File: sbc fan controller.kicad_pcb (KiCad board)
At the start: 2 copper layers, 46 x 53 mm, 23 parts, among them J1 Conn_01x13, J10 ISP-6, J2 Conn_01x02, J3 TEST_1P, J6 Conn_01x03, J7 TEST_1P, Q1 Q_PMOS_GSD, U1 ATTINY13A-SSU, U3 4N25

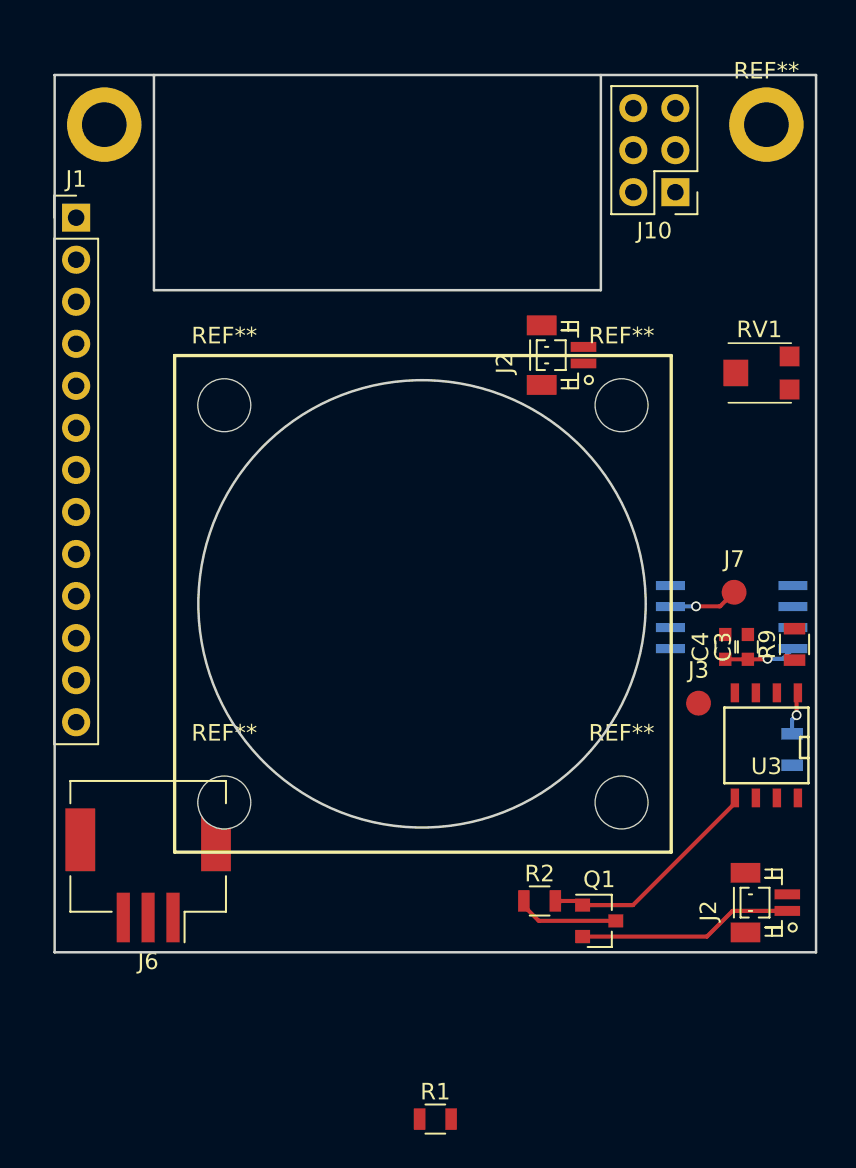
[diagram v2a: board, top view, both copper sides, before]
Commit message: Final layout
Simplified layout and tested each footprint with a hard copy layout actual parts.
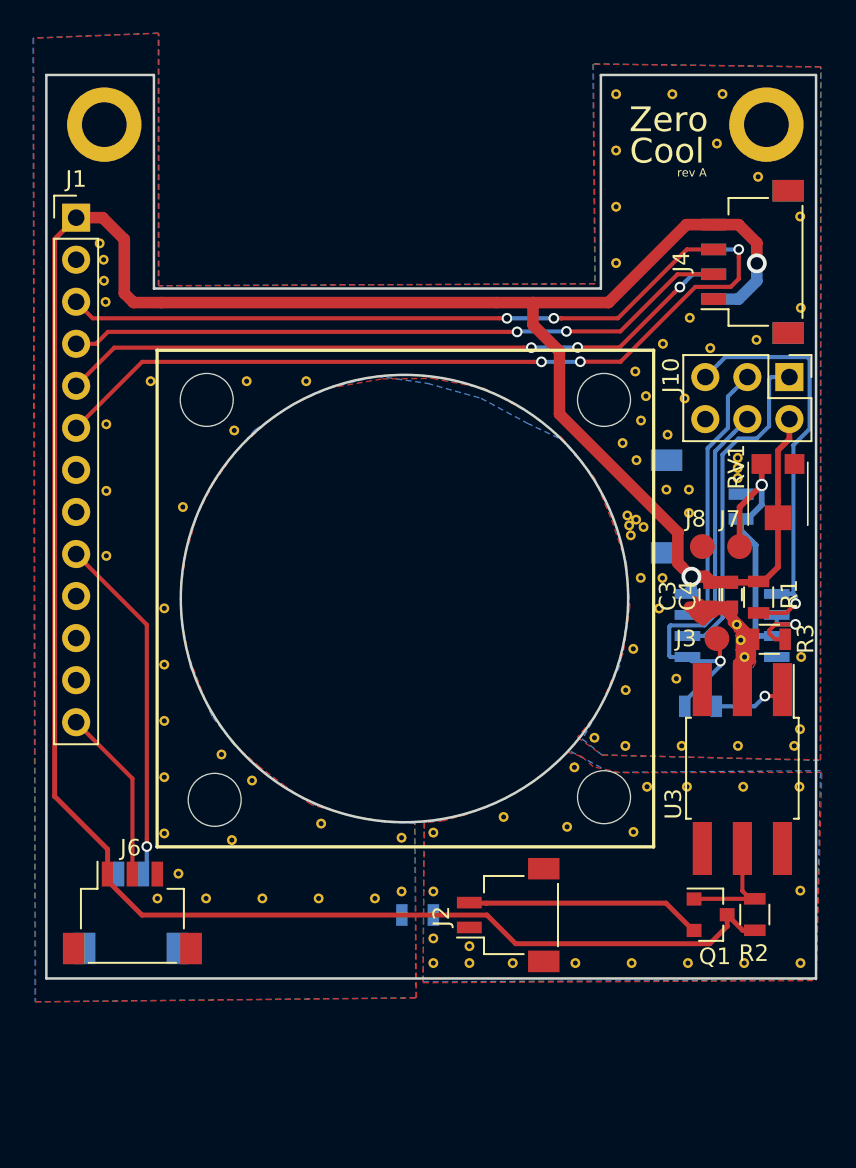
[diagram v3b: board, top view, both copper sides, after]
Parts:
- removed the J2 at (190.7, 56.9)
- removed the J2 at (203.0, 90.0)
- removed R9: 0R, Resistors_SMD:R_0805
- added J2: Conn_01x02, JST_test_2:JST_ZH_SM02B-ZRSS-TB_1x02_P1.50mm_Horizontal, F.Cu at (187.4, 90.8)
- added J4: Conn_01x04, JST_test_2:JST_ZH_SM04B-ZRSS-TB_1x04_P1.50mm_Horizontal, F.Cu at (202.2, 51.3)
- added J5: Conn_01x04, JST_test_2:JST_ZH_SM04B-ZRSS-TB_1x04_P1.50mm_Horizontal, B.Cu at (202.2, 51.3)
- added J8: TEST_1P, Measurement_Points:Measurement_Point_Round-SMD-Pad_Small, F.Cu at (199.1, 68.5)
- added J9: Conn_01x02, JST_test_2:JST_ZH_SM02B-ZRSS-TB_1x02_P1.50mm_Horizontal, B.Cu at (164.6, 90.6)
- added L1: Ferrite_Bead, Resistors_SMD:R_0805, B.Cu at (181.9, 90.8)
- added R3: 10k, Resistors_SMD:R_0805, F.Cu at (203.2, 74.1)
- added REF**: VIA-0.6mm, node_nrf:VIA-0.6mm, F.Cu at (201.2, 73.2)
- added REF**: VIA-0.6mm, node_nrf:VIA-0.6mm, F.Cu at (163.0, 52.4)
- added REF**: VIA-0.6mm, node_nrf:VIA-0.6mm, F.Cu at (205.1, 93.7)
- added REF**: VIA-0.6mm, node_nrf:VIA-0.6mm, F.Cu at (185.1, 93.7)
- added REF**: VIA-0.6mm, node_nrf:VIA-0.6mm, F.Cu at (185.1, 92.6)
- added REF**: VIA-0.6mm, node_nrf:VIA-0.6mm, F.Cu at (166.2, 89.8)
- added REF**: VIA-0.6mm, node_nrf:VIA-0.6mm, F.Cu at (163.1, 53.7)
- added REF**: VIA-0.6mm, node_nrf:VIA-0.6mm, F.Cu at (163.1, 65.1)
- added REF**: VIA-0.6mm, node_nrf:VIA-0.6mm, F.Cu at (163.1, 69.0)
- added REF**: VIA-0.6mm, node_nrf:VIA-0.6mm, F.Cu at (167.8, 66.1)
- added REF**: VIA-0.6mm, node_nrf:VIA-0.6mm, F.Cu at (170.8, 61.5)
- added REF**: VIA-0.6mm, node_nrf:VIA-0.6mm, F.Cu at (175.2, 58.5)
- added REF**: VIA-0.6mm, node_nrf:VIA-0.6mm, F.Cu at (201.4, 74.1)
- added REF**: VIA-0.6mm, node_nrf:VIA-0.6mm, F.Cu at (171.6, 58.5)
- added REF**: VIA-0.6mm, node_nrf:VIA-0.6mm, F.Cu at (165.8, 58.5)
- added REF**: VIA-0.6mm, node_nrf:VIA-0.6mm, F.Cu at (163.1, 61.1)
- added REF**: VIA-0.6mm, node_nrf:VIA-0.6mm, F.Cu at (166.6, 72.2)
- added REF**: VIA-0.6mm, node_nrf:VIA-0.6mm, F.Cu at (166.6, 75.6)
- added REF**: VIA-0.6mm, node_nrf:VIA-0.6mm, F.Cu at (166.6, 79.0)
- added REF**: VIA-0.6mm, node_nrf:VIA-0.6mm, F.Cu at (166.6, 82.4)
- added REF**: VIA-0.6mm, node_nrf:VIA-0.6mm, F.Cu at (166.6, 85.8)
- added REF**: VIA-0.6mm, node_nrf:VIA-0.6mm, F.Cu at (167.5, 88.2)
- added REF**: VIA-0.6mm, node_nrf:VIA-0.6mm, F.Cu at (170.1, 81.0)
- added REF**: VIA-0.6mm, node_nrf:VIA-0.6mm, F.Cu at (201.7, 75.2)
- added REF**: VIA-0.6mm, node_nrf:VIA-0.6mm, F.Cu at (170.7, 86.2)
- added REF**: VIA-0.6mm, node_nrf:VIA-0.6mm, F.Cu at (169.2, 89.7)
- added REF**: VIA-0.6mm, node_nrf:VIA-0.6mm, F.Cu at (172.6, 89.7)
- added REF**: VIA-0.6mm, node_nrf:VIA-0.6mm, F.Cu at (175.9, 89.7)
- added REF**: VIA-0.6mm, node_nrf:VIA-0.6mm, F.Cu at (171.9, 82.6)
- added REF**: VIA-0.6mm, node_nrf:VIA-0.6mm, F.Cu at (176.1, 85.2)
- added REF**: VIA-0.6mm, node_nrf:VIA-0.6mm, F.Cu at (179.3, 89.7)
- added REF**: VIA-0.6mm, node_nrf:VIA-0.6mm, F.Cu at (181.0, 89.3)
- added REF**: VIA-0.6mm, node_nrf:VIA-0.6mm, F.Cu at (181.0, 86.1)
- added REF**: VIA-0.6mm, node_nrf:VIA-0.6mm, F.Cu at (195.0, 85.7)
- added REF**: VIA-0.6mm, node_nrf:VIA-0.6mm, F.Cu at (196.5, 72.2)
- added REF**: VIA-0.6mm, node_nrf:VIA-0.6mm, F.Cu at (191.4, 81.8)
- added REF**: VIA-0.6mm, node_nrf:VIA-0.6mm, F.Cu at (187.1, 84.8)
- added REF**: VIA-0.6mm, node_nrf:VIA-0.6mm, F.Cu at (182.9, 85.8)
- added REF**: VIA-0.6mm, node_nrf:VIA-0.6mm, F.Cu at (182.9, 89.3)
- added REF**: VIA-0.6mm, node_nrf:VIA-0.6mm, F.Cu at (182.9, 92.2)
- added REF**: VIA-0.6mm, node_nrf:VIA-0.6mm, F.Cu at (187.7, 93.7)
- added REF**: VIA-0.6mm, node_nrf:VIA-0.6mm, F.Cu at (182.9, 93.7)
- added REF**: VIA-0.6mm, node_nrf:VIA-0.6mm, F.Cu at (205.1, 89.3)
- added REF**: VIA-0.6mm, node_nrf:VIA-0.6mm, F.Cu at (200.3, 41.1)
- added REF**: VIA-0.6mm, node_nrf:VIA-0.6mm, F.Cu at (197.3, 41.2)
- added REF**: VIA-0.6mm, node_nrf:VIA-0.6mm, F.Cu at (196.7, 70.4)
- added REF**: VIA-0.6mm, node_nrf:VIA-0.6mm, F.Cu at (193.9, 41.2)
- added REF**: VIA-0.6mm, node_nrf:VIA-0.6mm, F.Cu at (193.9, 44.6)
- added REF**: VIA-0.6mm, node_nrf:VIA-0.6mm, F.Cu at (193.9, 48.0)
- added REF**: VIA-0.6mm, node_nrf:VIA-0.6mm, F.Cu at (198.3, 66.5)
- added REF**: VIA-0.6mm, node_nrf:VIA-0.6mm, F.Cu at (195.4, 70.4)
- added REF**: VIA-0.6mm, node_nrf:VIA-0.6mm, F.Cu at (195.1, 66.9)
- added REF**: VIA-0.6mm, node_nrf:VIA-0.6mm, F.Cu at (195.6, 67.3)
- added REF**: VIA-0.6mm, node_nrf:VIA-0.6mm, F.Cu at (194.8, 67.8)
- added REF**: VIA-0.6mm, node_nrf:VIA-0.6mm, F.Cu at (194.7, 67.2)
- added REF**: VIA-0.6mm, node_nrf:VIA-0.6mm, F.Cu at (204.7, 80.5)
- added REF**: VIA-0.6mm, node_nrf:VIA-0.6mm, F.Cu at (205.1, 75.2)
- added REF**: VIA-0.6mm, node_nrf:VIA-0.6mm, F.Cu at (201.3, 80.5)
- added REF**: VIA-0.6mm, node_nrf:VIA-0.6mm, F.Cu at (197.9, 80.5)
- added REF**: VIA-0.6mm, node_nrf:VIA-0.6mm, F.Cu at (195.8, 83.0)
- added REF**: VIA-0.6mm, node_nrf:VIA-0.6mm, F.Cu at (198.2, 83.0)
- added REF**: VIA-0.6mm, node_nrf:VIA-0.6mm, F.Cu at (201.6, 83.0)
- added REF**: VIA-0.6mm, node_nrf:VIA-0.6mm, F.Cu at (205.0, 83.0)
- added REF**: VIA-0.6mm, node_nrf:VIA-0.6mm, F.Cu at (191.5, 93.7)
- added REF**: VIA-0.6mm, node_nrf:VIA-0.6mm, F.Cu at (194.9, 93.7)
- added REF**: VIA-0.6mm, node_nrf:VIA-0.6mm, F.Cu at (198.3, 93.7)
- added REF**: VIA-0.6mm, node_nrf:VIA-0.6mm, F.Cu at (201.7, 93.7)
- added REF**: VIA-0.6mm, node_nrf:VIA-0.6mm, F.Cu at (191.0, 85.4)
- added REF**: VIA-0.6mm, node_nrf:VIA-0.6mm, F.Cu at (201.3, 63.1)
- added REF**: VIA-0.6mm, node_nrf:VIA-0.6mm, F.Cu at (201.3, 63.7)
- added REF**: VIA-0.6mm, node_nrf:VIA-0.6mm, F.Cu at (197.6, 76.5)
- added REF**: VIA-0.6mm, node_nrf:VIA-0.6mm, F.Cu at (205.0, 79.5)
- added REF**: VIA-0.6mm, node_nrf:VIA-0.6mm, F.Cu at (194.5, 77.2)
- added REF**: VIA-0.6mm, node_nrf:VIA-0.6mm, F.Cu at (194.5, 80.5)
- added REF**: VIA-0.6mm, node_nrf:VIA-0.6mm, F.Cu at (192.6, 80.0)
- added REF**: VIA-0.6mm, node_nrf:VIA-0.6mm, F.Cu at (195.0, 74.7)
- added REF**: VIA-0.6mm, node_nrf:VIA-0.6mm, F.Cu at (194.6, 66.6)
- added REF**: VIA-0.6mm, node_nrf:VIA-0.6mm, F.Cu at (198.3, 65.0)
- added REF**: VIA-0.6mm, node_nrf:VIA-0.6mm, F.Cu at (162.7, 50.2)
- added REF**: VIA-0.6mm, node_nrf:VIA-0.6mm, F.Cu at (197.0, 65.0)
- added REF**: VIA-0.6mm, node_nrf:VIA-0.6mm, F.Cu at (197.0, 61.7)
- added REF**: VIA-0.6mm, node_nrf:VIA-0.6mm, F.Cu at (198.1, 59.5)
- added REF**: VIA-0.6mm, node_nrf:VIA-0.6mm, F.Cu at (199.6, 56.5)
- added REF**: VIA-0.6mm, node_nrf:VIA-0.6mm, F.Cu at (202.4, 56.0)
- added REF**: VIA-0.6mm, node_nrf:VIA-0.6mm, F.Cu at (205.1, 54.1)
- added REF**: VIA-0.6mm, node_nrf:VIA-0.6mm, F.Cu at (205.0, 48.5)
- added REF**: VIA-0.6mm, node_nrf:VIA-0.6mm, F.Cu at (202.5, 46.1)
- added REF**: VIA-0.6mm, node_nrf:VIA-0.6mm, F.Cu at (200.0, 44.1)
- added REF**: VIA-0.6mm, node_nrf:VIA-0.6mm, F.Cu at (193.9, 51.4)
- added REF**: VIA-0.6mm, node_nrf:VIA-0.6mm, F.Cu at (163.0, 51.2)
- added REF**: VIA-0.6mm, node_nrf:VIA-0.6mm, F.Cu at (196.8, 56.2)
- added REF**: VIA-0.6mm, node_nrf:VIA-0.6mm, F.Cu at (198.4, 54.7)
- added REF**: VIA-0.6mm, node_nrf:VIA-0.6mm, F.Cu at (195.7, 59.4)
- added REF**: VIA-0.6mm, node_nrf:VIA-0.6mm, F.Cu at (195.1, 57.9)
- added REF**: VIA-0.6mm, node_nrf:VIA-0.6mm, F.Cu at (195.4, 60.9)
- added REF**: VIA-0.6mm, node_nrf:VIA-0.6mm, F.Cu at (195.2, 63.3)
- added REF**: VIA-0.6mm, node_nrf:VIA-0.6mm, F.Cu at (194.3, 62.2)
- added REF**: VIA-0.6mm, node_nrf:VIA-0.6mm, F.Cu at (201.3, 64.3)
- added TH1: 10k, JST_test_2:JST_ZH_SM02B-ZRSS-TB_1x02_P1.50mm_Horizontal, B.Cu at (199.1, 66.1)
- J6: footprint Connectors_JST:JST_ZE_SM03B-ZESS-TB_03x1.5mm_Angled -> JST_test_2:JST_ZH_SM03B-ZRSS-TB_1x03_P1.50mm_Horizontal
- U1: footprint Housings_SOIC:SO-8_5.3x6.2mm_Pitch1.27mm -> Housings_SOIC:SOIC-8_3.9x4.9mm_Pitch1.27mm
- U3: footprint SMD_Packages:SOIC-8-N -> 4n25_sop6:SO-6_4.4x3.6mm_Pitch1.27mm
- moved R1 37.1 mm to (202.5, 71.5), turned to 270 degrees
- moved J10 13.1 mm to (204.4, 58.2), turned to 270 degrees
- moved R2 13.0 mm to (202.3, 90.7), turned to 90 degrees
- moved RV1 7.38 mm to (203.7, 65.3), turned to 180 degrees
- moved Q1 6.74 mm to (199.6, 90.7)
- moved R5 6.11 mm to (199.0, 78.1), turned to 180 degrees
- moved J3 4.05 mm to (200.0, 74.0)
- moved C3 3.91 mm to (199.6, 71.4), turned to 270 degrees
- moved C4 3.18 mm to (200.9, 71.4), turned to 270 degrees
- moved J7 2.78 mm to (201.4, 68.5)
- moved J6 2.28 mm to (164.7, 90.6), turned to 0 degrees
- moved U3 2.04 mm to (201.6, 81.9), turned to 270 degrees
- moved REF** 1.11 mm to (193.2, 83.6)
- moved REF** 1.11 mm to (169.2, 59.6)
- moved REF** 1.11 mm to (193.2, 59.6)
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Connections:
- U1 pad 2: Net-(U1-Pad2) -> /FLT
- U3 pad 2: Net-(R9-Pad1) -> GND
- U3 pad 4: GND -> Earth_Clean
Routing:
- net +5V: track 10.6 -> 174.2 mm, vias 1 -> 2
- net /USB2+: track 0.00 -> 47.0 mm, vias 0 -> 3
- net /USB2-: track 0.00 -> 41.3 mm, vias 0 -> 3
- net /USB1-: track 0.00 -> 40.7 mm, vias 0 -> 2
- net /USB1+: track 0.00 -> 40.3 mm, vias 0 -> 2
- net GND: track 0.00 -> 30.6 mm
- net /RST: track 0.00 -> 26.5 mm, vias 0 -> 1
- net /ISO: track 0.04 -> 25.6 mm, vias 0 -> 1
- net /TV_OUT: track 0.00 -> 21.2 mm, vias 0 -> 1
- net /MISO: track 0.00 -> 20.1 mm
- net /SCK: track 0.60 -> 16.5 mm
- net /SIG: track 4.21 -> 17.0 mm
- net /IR_RX: track 0.00 -> 10.6 mm
- net Net-(Q1-Pad1): track 13.8 -> 7.19 mm
- net /FLT: track 0.00 -> 4.73 mm, vias 0 -> 1
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- added copper zone on B.Cu, net Earth_Clean
- added copper zone on F.Cu, net Earth_Clean
- added copper zone on B.Cu, net GND
- added copper zone on F.Cu, net GND
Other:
- board size 46 x 53 mm -> 46.5 x 54.6 mm
- net class Default: via_dia 0.6 -> 0.65
- net class Power added: clearance 0.25, trace_width 0.7, via_dia 1.2, via_drill 0.755
- net class analog added: clearance 0.2, trace_width 0.35, via_dia 0.75, via_drill 0.5
- rule trace_min: 0.2 -> 0.1524
- rule via_min_drill: 0.3 -> 0.254
- rule via_min_size: 0.4 -> 0.127
- board text added: "2017-12-23"
- board text added: "CUT OUT"
- board text added: "Cool"
- board text added: "Zero"
- board text added: "cms@dreaming.org"
- board text added: "rev A"
